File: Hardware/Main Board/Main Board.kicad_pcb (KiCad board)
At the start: 2 copper layers, 78.7 x 29.1 mm, 59 parts, among them Q1 MMBT3904-TP, Q2 MMBT3904-TP, Q3 AO4484, SW1 Momentary, U1 MT3608, U2 NCP718A, U3 ATtiny1614, U4 TP4056

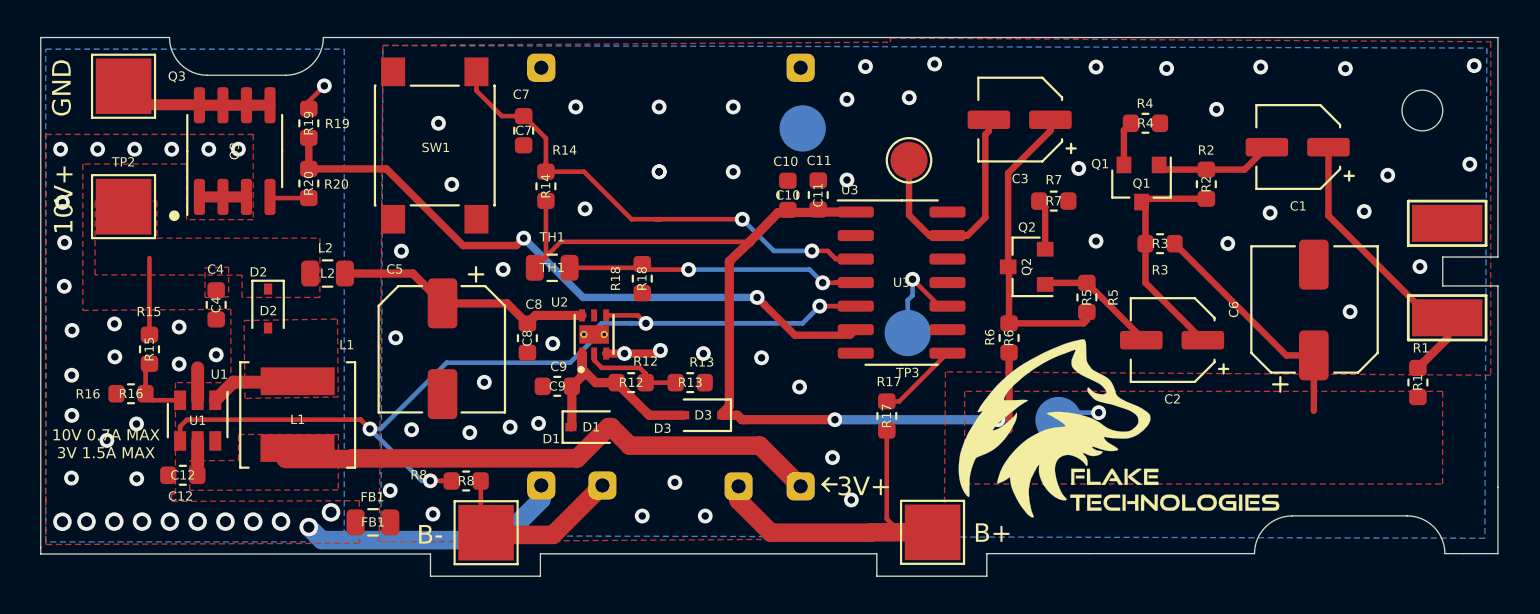
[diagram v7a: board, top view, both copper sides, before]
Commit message: board review done, almost done BOM and component map.
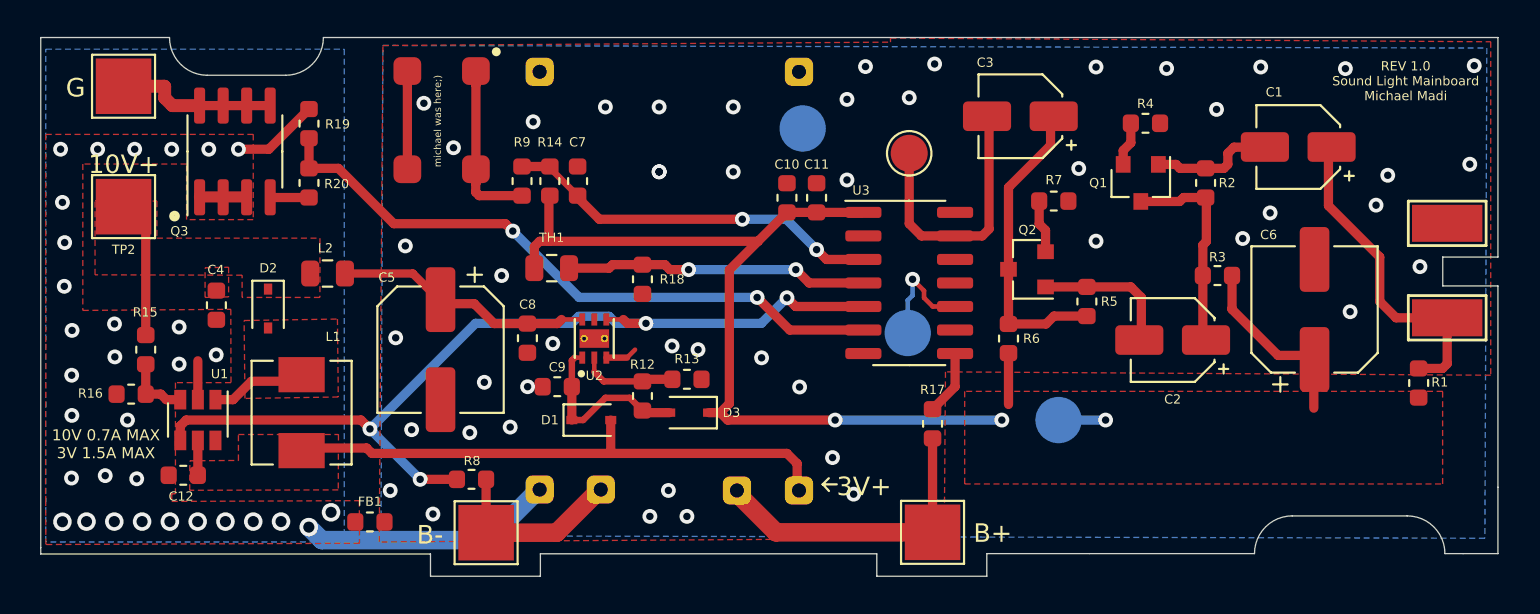
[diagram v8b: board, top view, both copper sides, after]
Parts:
- removed G***: LOGO, 123332343423
- removed G***: LOGO, 1
- removed G***: LOGO, 3333
- removed G***: LOGO, ddr
- removed REF**: MountingHole_2.2mm_M2, MountingHole:MountingHole_2.2mm_M2
- added R9: 1k, Resistor_SMD:R_0603_1608Metric, F.Cu at (133.1, 91.5)
- C1, C2, C3: footprint Main Board:CP_Elec_4x3 -> Capacitor_SMD:CP_Elec_4x5.3
- C5, C6: footprint Main Board:100 -> Capacitor_SMD:CP_Elec_6.3x7.7
- FB1: footprint Resistor_SMD:R_0805_2012Metric -> Resistor_SMD:R_0603_1608Metric
- L1: footprint Main Board:BW10uHInductor -> Inductor_SMD:L_Sunlord_MWSA0518_5.4x5.2mm
- SW1: footprint Button_Switch_SMD:SW_SPST_PTS645 -> Main Board1:tactile
- moved C7 3.98 mm to (136.1, 91.5), turned to 90 degrees
- moved R3 3.54 mm to (170.6, 96.6)
- moved R17 2.51 mm to (155.3, 104.6)
- moved SW1 1.98 mm to (129.0, 87.7), turned to 270 degrees
- moved R12 0.94 mm to (139.6, 103.1), turned to 90 degrees
- moved D3 0.77 mm to (142.1, 104.0)
- moved L1 0.43 mm to (121.2, 104.0)
- moved U3 0.41 mm to (154.0, 97.0)
- moved D1 0.38 mm to (136.8, 104.4)
- moved TP8 0.38 mm to (154.0, 90.0)
- moved R14 0.35 mm to (134.6, 91.5)
- moved R8 0.30 mm to (130.4, 107.6)
- moved R13 0.25 mm to (142.0, 102.2)
- moved U4 0.24 mm to (148.5, 111.8)
- moved U2 0.22 mm to (137.0, 100.0)
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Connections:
- SW1 pad 2: /MODE -> Net-(R9-Pad2)
- U1 pad 6: Net-(U1-Pad6) -> (no net)
- U3 pad 11: Net-(U3-Pad11) -> (no net)
- U3 pad 12: Net-(U3-Pad12) -> (no net)
- U3 pad 2: Net-(U3-Pad2) -> (no net)
- U3 pad 7: Net-(U3-Pad7) -> (no net)
- U3 pad 9: Net-(U3-Pad9) -> (no net)
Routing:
- net Net-(R9-Pad2): track 0.00 -> 9.12 mm
- net /MODE: track 27.1 -> 20.8 mm
- net GNDA: track 3.05 -> 7.03 mm, vias 49 -> 48
- net +5V: track 67.1 -> 63.7 mm
- net +10V: track 4.14 -> 7.43 mm
- net +BATT: track 19.5 -> 16.6 mm
- net GNDPWR: track 20.4 -> 23.1 mm, vias 33 -> 32
- net Net-(C9-Pad1): track 11.9 -> 9.95 mm
- net Net-(C2-Pad2): track 6.60 -> 7.87 mm
- net Net-(C1-Pad1): track 16.6 -> 17.7 mm
- net Net-(C2-Pad1): track 12.4 -> 11.3 mm
- net /PACK_SENSE: track 4.35 -> 3.51 mm
- net +3V3: track 31.7 -> 32.5 mm
- net /D: track 7.92 -> 8.74 mm
- net /EN: track 48.7 -> 49.5 mm
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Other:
- board text added: "REV 1.0 Sound Light Mainboard Michael Madi"
- board text removed: "GND"
